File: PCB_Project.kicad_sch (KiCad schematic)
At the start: 0 parts

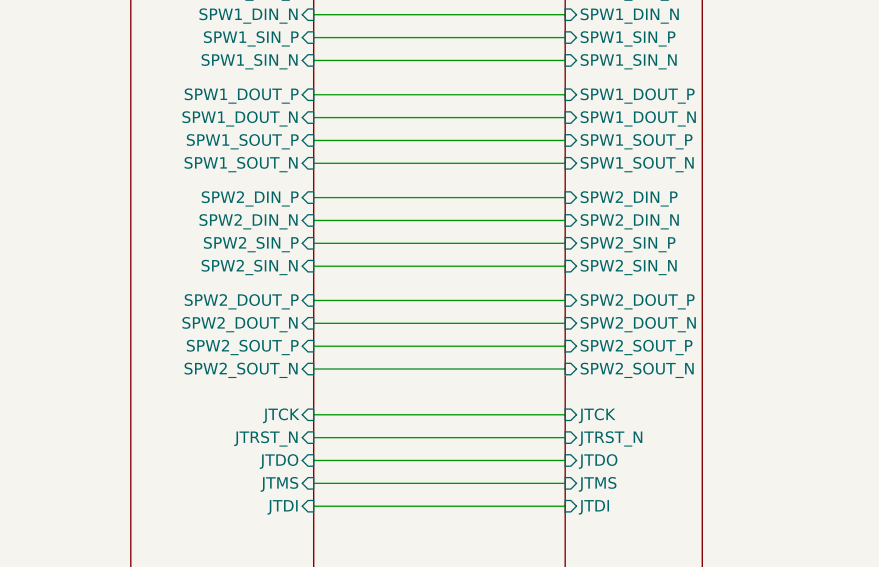
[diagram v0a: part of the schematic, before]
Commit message: added MAX, picoblade, NPN
added the LDO (placement), added the picoblade connector for CFG and deleted one SPW out of 2 in the DF9.
added the NPN transistor (placed)
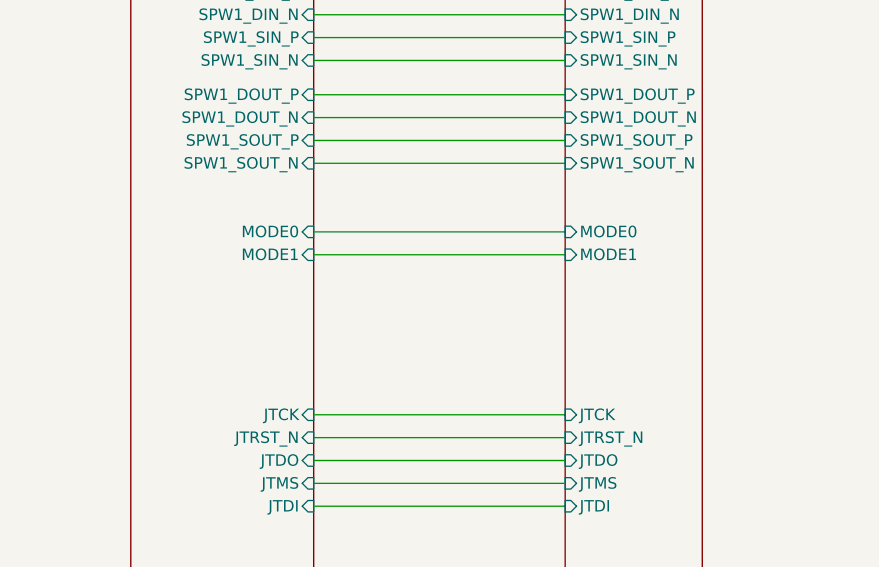
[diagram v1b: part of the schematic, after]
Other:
- sheet 02_FPGA_Config_JTAG_Bitstream_Reset ports: added MODE0, MODE1; removed SPW2_DIN_N, SPW2_DIN_P, SPW2_DOUT_N, SPW2_DOUT_P, SPW2_SIN_N, SPW2_SIN_P, SPW2_SOUT_N, SPW2_SOUT_P
- sheet DF9_CFG-SPW ports: added MODE0, MODE1; removed SPW2_DIN_N, SPW2_DIN_P, SPW2_DOUT_N, SPW2_DOUT_P, SPW2_SIN_N, SPW2_SIN_P, SPW2_SOUT_N, SPW2_SOUT_P
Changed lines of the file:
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@@
-	(wire
-		(pts
-			(xy 78.74 52.07) (xy 106.68 52.07)
-		)
-		(stroke
-			(width 0)
-			(type default)
-		)
-	)
 	(wire
 		(pts
@@
 	(wire
 		(pts
-			(xy 78.74 54.61) (xy 106.68 54.61)
-		)
-		(stroke
-			(width 0)
-			(type default)
-		)
-	)
-	(wire
-		(pts
 			(xy 78.74 48.26) (xy 106.68 48.26)
 		)
@@
 	(wire
 		(pts
-			(xy 78.74 57.15) (xy 106.68 57.15)
-		)
-		(stroke
-			(width 0)
-			(type default)
-		)
-	)
-	(wire
-		(pts
 			(xy 78.74 43.18) (xy 106.68 43.18)
 		)
@@
 	(wire
 		(pts
-			(xy 78.74 66.04) (xy 106.68 66.04)
-		)
-		(stroke
-			(width 0)
-			(type default)
-		)
-	)
-	(wire
-		(pts
 			(xy 78.74 36.83) (xy 106.68 36.83)
 		)
@@
 	(wire
 		(pts
-			(xy 78.74 68.58) (xy 106.68 68.58)
-		)
-		(stroke
-			(width 0)
-			(type default)
-		)
-	)
-	(wire
-		(pts
-			(xy 78.74 63.5) (xy 106.68 63.5)
+			(xy 78.74 58.42) (xy 106.68 58.42)
 		)
 		(stroke
@@
 	(wire
 		(pts
-			(xy 78.74 71.12) (xy 106.68 71.12)
-		)
-		(stroke
-			(width 0)
-			(type default)
-		)
-	)
-	(wire
-		(pts
-			(xy 78.74 59.69) (xy 106.68 59.69)
+			(xy 78.74 55.88) (xy 106.68 55.88)
 		)
 		(stroke
@@
 			)
 		)
-		(pin "SPW2_DIN_P" input
-			(at 106.68 52.07 180)
-			(effects
-				(font
-					(size 1.27 1.27)
-				)
-				(justify left)
-			)
-		)
-		(pin "SPW2_DOUT_P" input
-			(at 106.68 63.5 180)
-			(effects
-				(font
-					(size 1.27 1.27)
-				)
-				(justify left)
-			)
-		)
-		(pin "SPW2_SIN_N" input
-			(at 106.68 59.69 180)
-			(effects
-				(font
-					(size 1.27 1.27)
-				)
-				(justify left)
-			)
-		)
-		(pin "SPW2_DIN_N" input
-			(at 106.68 54.61 180)
-			(effects
-				(font
-					(size 1.27 1.27)
-				)
-				(justify left)
-			)
-		)
 		(pin "JTMS" input
 			(at 106.68 83.82 180)
@@
 			)
 		)
-		(pin "SPW2_DOUT_N" input
-			(at 106.68 66.04 180)
-			(effects
-				(font
-					(size 1.27 1.27)
-				)
-				(justify left)
-			)
-		)
 		(pin "JTDO" input
 			(at 106.68 81.28 180)
@@
 			)
 		)
-		(pin "SPW2_SOUT_P" input
-			(at 106.68 68.58 180)
-			(effects
-				(font
-					(size 1.27 1.27)
-				)
-				(justify left)
-			)
-		)
 		(pin "JTRST_N" input
 			(at 106.68 78.74 180)
@@
 			)
 		)
-		(pin "SPW2_SIN_P" input
-			(at 106.68 57.15 180)
-			(effects
-				(font
-					(size 1.27 1.27)
-				)
-				(justify left)
-			)
-		)
 		(pin "JTDI" input
 			(at 106.68 86.36 180)
@@
 			)
 		)
-		(pin "SPW2_SOUT_N" input
-			(at 106.68 71.12 180)
-			(effects
-				(font
-					(size 1.27 1.27)
-				)
-				(justify left)
-			)
-		)
 		(pin "JTCK" input
 			(at 106.68 76.2 180)
+			(effects
+				(font
+					(size 1.27 1.27)
+				)
+				(justify left)
+			)
+		)
+		(pin "MODE0" input
+			(at 106.68 55.88 180)
+			(effects
+				(font
+					(size 1.27 1.27)
+				)
+				(justify left)
+			)
+		)
+		(pin "MODE1" input
+			(at 106.68 58.42 180)
 			(effects
 				(font
@@
 			)
 		)
-		(pin "SPW2_DOUT_N" input
-			(at 78.74 66.04 0)
-			(effects
-				(font
-					(size 1.27 1.27)
-				)
-				(justify right)
-			)
-		)
 		(pin "JTMS" input
 			(at 78.74 83.82 0)
@@
 			)
 		)
-		(pin "SPW2_SOUT_P" input
-			(at 78.74 68.58 0)
-			(effects
-				(font
-					(size 1.27 1.27)
-				)
-				(justify right)
-			)
-		)
-		(pin "SPW2_DIN_N" input
-			(at 78.74 54.61 0)
-			(effects
-				(font
-					(size 1.27 1.27)
-				)
-				(justify right)
-			)
-		)
-		(pin "SPW2_SIN_N" input
-			(at 78.74 59.69 0)
-			(effects
-				(font
-					(size 1.27 1.27)
-				)
-				(justify right)
-			)
-		)
-		(pin "SPW2_SOUT_N" input
-			(at 78.74 71.12 0)
-			(effects
-				(font
-					(size 1.27 1.27)
-				)
-				(justify right)
-			)
-		)
-		(pin "SPW2_SIN_P" input
-			(at 78.74 57.15 0)
-			(effects
-				(font
-					(size 1.27 1.27)
-				)
-				(justify right)
-			)
-		)
-		(pin "SPW2_DIN_P" input
-			(at 78.74 52.07 0)
-			(effects
-				(font
-					(size 1.27 1.27)
-				)
-				(justify right)
-			)
-		)
-		(pin "SPW2_DOUT_P" input
-			(at 78.74 63.5 0)
-			(effects
-				(font
+		(pin "MODE0" input
+			(at 78.74 55.88 0)
+			(effects
+				(font
+					(size 1.27 1.27)
+				)
+				(justify right)
+			)
+		)
+		(pin "MODE1" input
+			(at 78.74 58.42 0)
+			(effects
+				(font

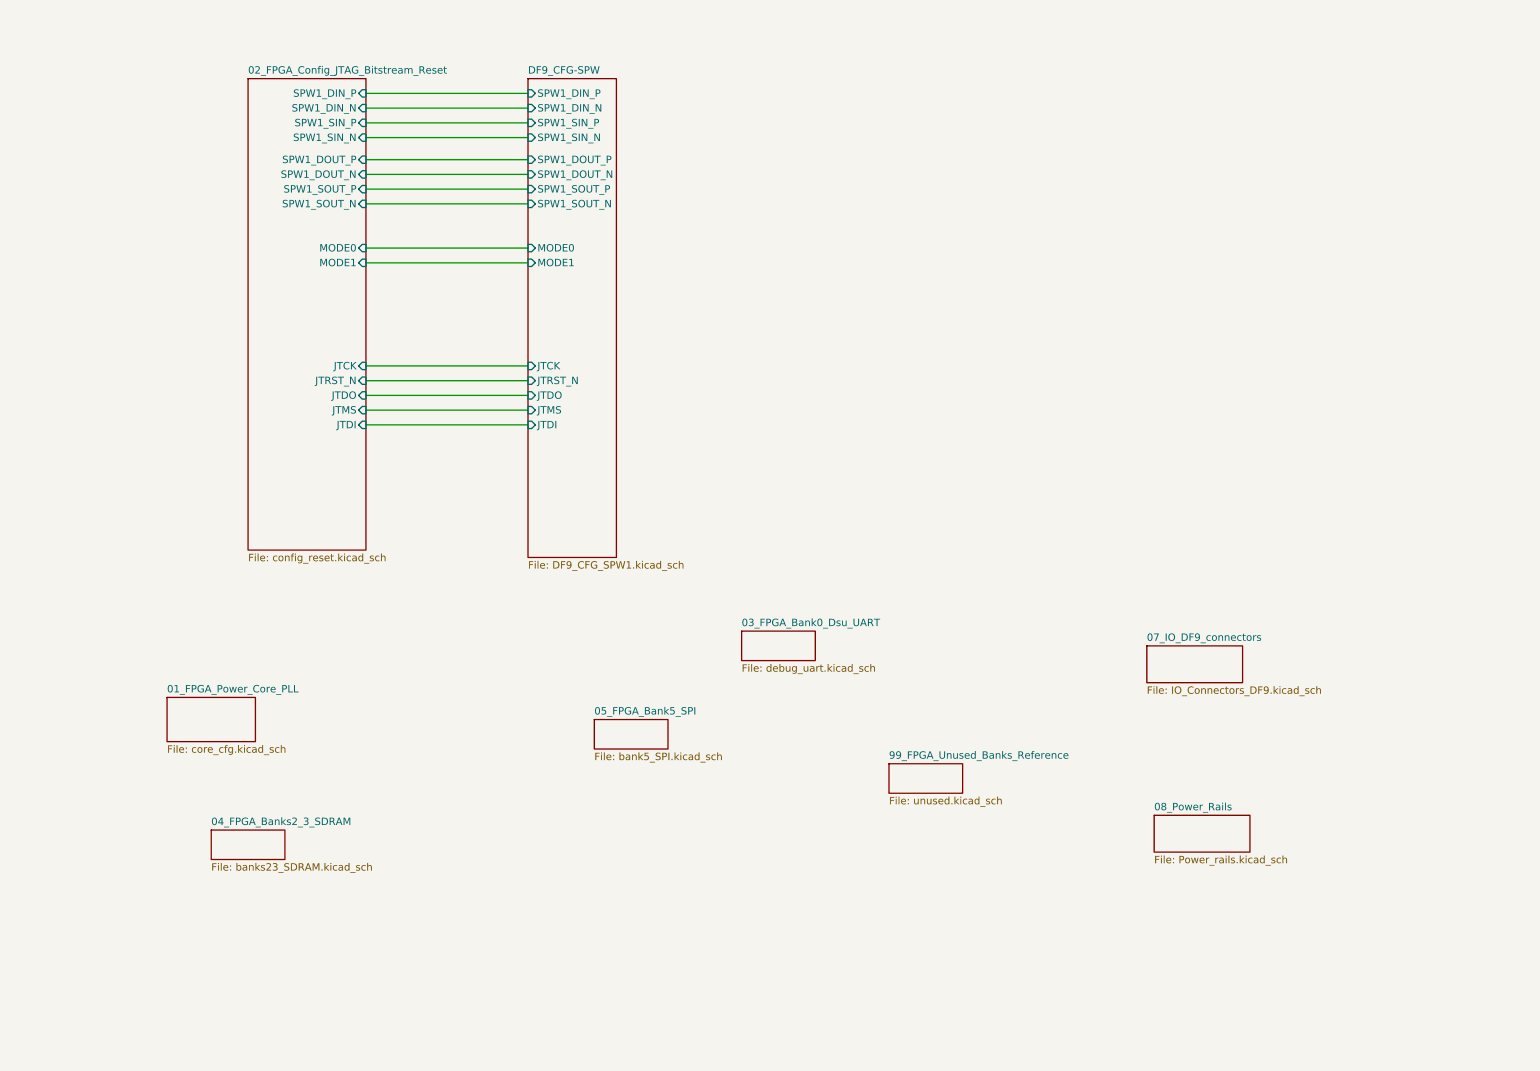
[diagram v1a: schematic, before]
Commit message: CFG, bga sdram, banks to connectors, docoupling
Finished completely routing bga sdram, finished tracing Banks to connectors DF9. Finished tracing Picoblade, diode, reset supervisor. Finished tracing LEDS on bank 5. Finished decoupling all banks and core. Missing only the power tree and power rail level decoupling.
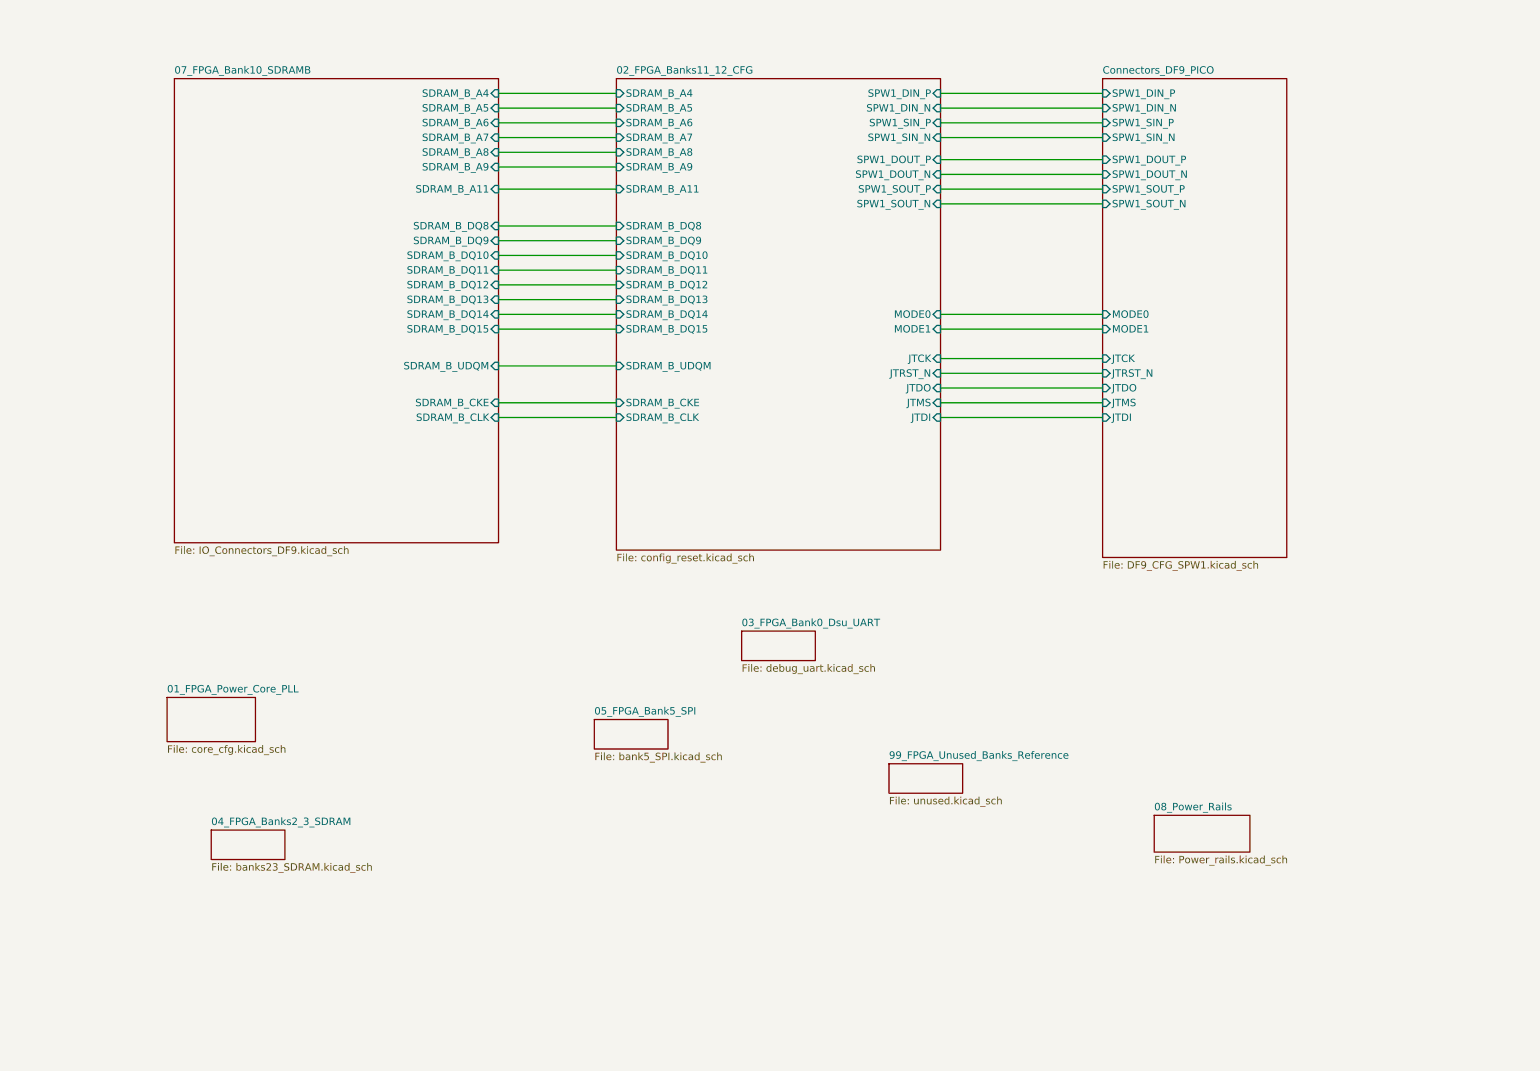
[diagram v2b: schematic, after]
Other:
- sheet 02_FPGA_Config_JTAG_Bitstream_Reset renamed 02_FPGA_Banks11_12_CFG
- sheet 07_IO_DF9_connectors renamed 07_FPGA_Bank10_SDRAMB
- sheet DF9_CFG-SPW renamed Connectors_DF9_PICO
- sheet 02_FPGA_Banks11_12_CFG ports: added SDRAM_B_A11, SDRAM_B_A4, SDRAM_B_A5, SDRAM_B_A6, SDRAM_B_A7, SDRAM_B_A8, SDRAM_B_A9, SDRAM_B_CKE, SDRAM_B_CLK, SDRAM_B_DQ10, SDRAM_B_DQ11, SDRAM_B_DQ12, SDRAM_B_DQ13, SDRAM_B_DQ14, SDRAM_B_DQ15, SDRAM_B_DQ8, SDRAM_B_DQ9, SDRAM_B_UDQM; removed none
- sheet 07_FPGA_Bank10_SDRAMB ports: added SDRAM_B_A11, SDRAM_B_A4, SDRAM_B_A5, SDRAM_B_A6, SDRAM_B_A7, SDRAM_B_A8, SDRAM_B_A9, SDRAM_B_CKE, SDRAM_B_CLK, SDRAM_B_DQ10, SDRAM_B_DQ11, SDRAM_B_DQ12, SDRAM_B_DQ13, SDRAM_B_DQ14, SDRAM_B_DQ15, SDRAM_B_DQ8, SDRAM_B_DQ9, SDRAM_B_UDQM; removed none

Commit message: power tree
power tree defined. Few changes remaining but almost finalized
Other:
- sheet 01_FPGA_Power_Core_PLL renamed FPGA_Core_PLL
- sheet 02_FPGA_Banks11_12_CFG renamed FPGA_Banks11_12_CFG
- sheet 03_FPGA_Bank0_Dsu_UART renamed FPGA_Bank0
- sheet 04_FPGA_Banks2_3_SDRAM renamed FPGA_Banks2_3_SDRAM
- sheet 05_FPGA_Bank5_SPI renamed FPGA_Bank5_SPI
- sheet 07_FPGA_Bank10_SDRAMB renamed FPGA_Bank10_SDRAMB
- sheet 08_Power_Rails renamed Rails_Decoupling
- sheet 99_FPGA_Unused_Banks_Reference renamed Power_Tree_LDOs
- sheet Connectors_DF9_PICO ports: added B0_01N_DF9, B0_01P_DF9, B0_02N_DF9, B0_02P_DF9, B0_03N_DF9, B0_03P_DF9, B0_04N_DF9, B0_04P_DF9, B0_05P_DF9, B0_06N_DF9, B0_06P_DF9, B0_07N_DF9, B0_07P_DF9, B0_08P_DF9, B0_09N_DF9, B0_09P_DF9, B0_10N_DF9, B0_10P_DF9, B0_11P_DF9, B5_03N_DF9, B5_03P_DF9, B5_04N_DF9, B5_07N_DF9, B5_08N_DF9, B5_08P_DF9, B5_09N_DF9, B5_10N_DF9, B5_10P_DF9, B5_11N_DF9, B5_11P_DF9, B5_12N_DF9, B5_12P_DF9, B5_13N_DF9; removed none
- sheet FPGA_Bank0 ports: added B0_01N_DF9, B0_01P_DF9, B0_02N_DF9, B0_02P_DF9, B0_03N_DF9, B0_03P_DF9, B0_04N_DF9, B0_04P_DF9, B0_05P_DF9, B0_06N_DF9, B0_06P_DF9, B0_07N_DF9, B0_07P_DF9, B0_08P_DF9, B0_09N_DF9, B0_09P_DF9, B0_10N_DF9, B0_10P_DF9, B0_11P_DF9; removed none
- sheet FPGA_Bank5_SPI ports: added B5_03N_DF9, B5_03P_DF9, B5_04N_DF9, B5_07N_DF9, B5_08N_DF9, B5_08P_DF9, B5_09N_DF9, B5_10N_DF9, B5_10P_DF9, B5_11N_DF9, B5_11P_DF9, B5_12N_DF9, B5_12P_DF9, B5_13N_DF9; removed none

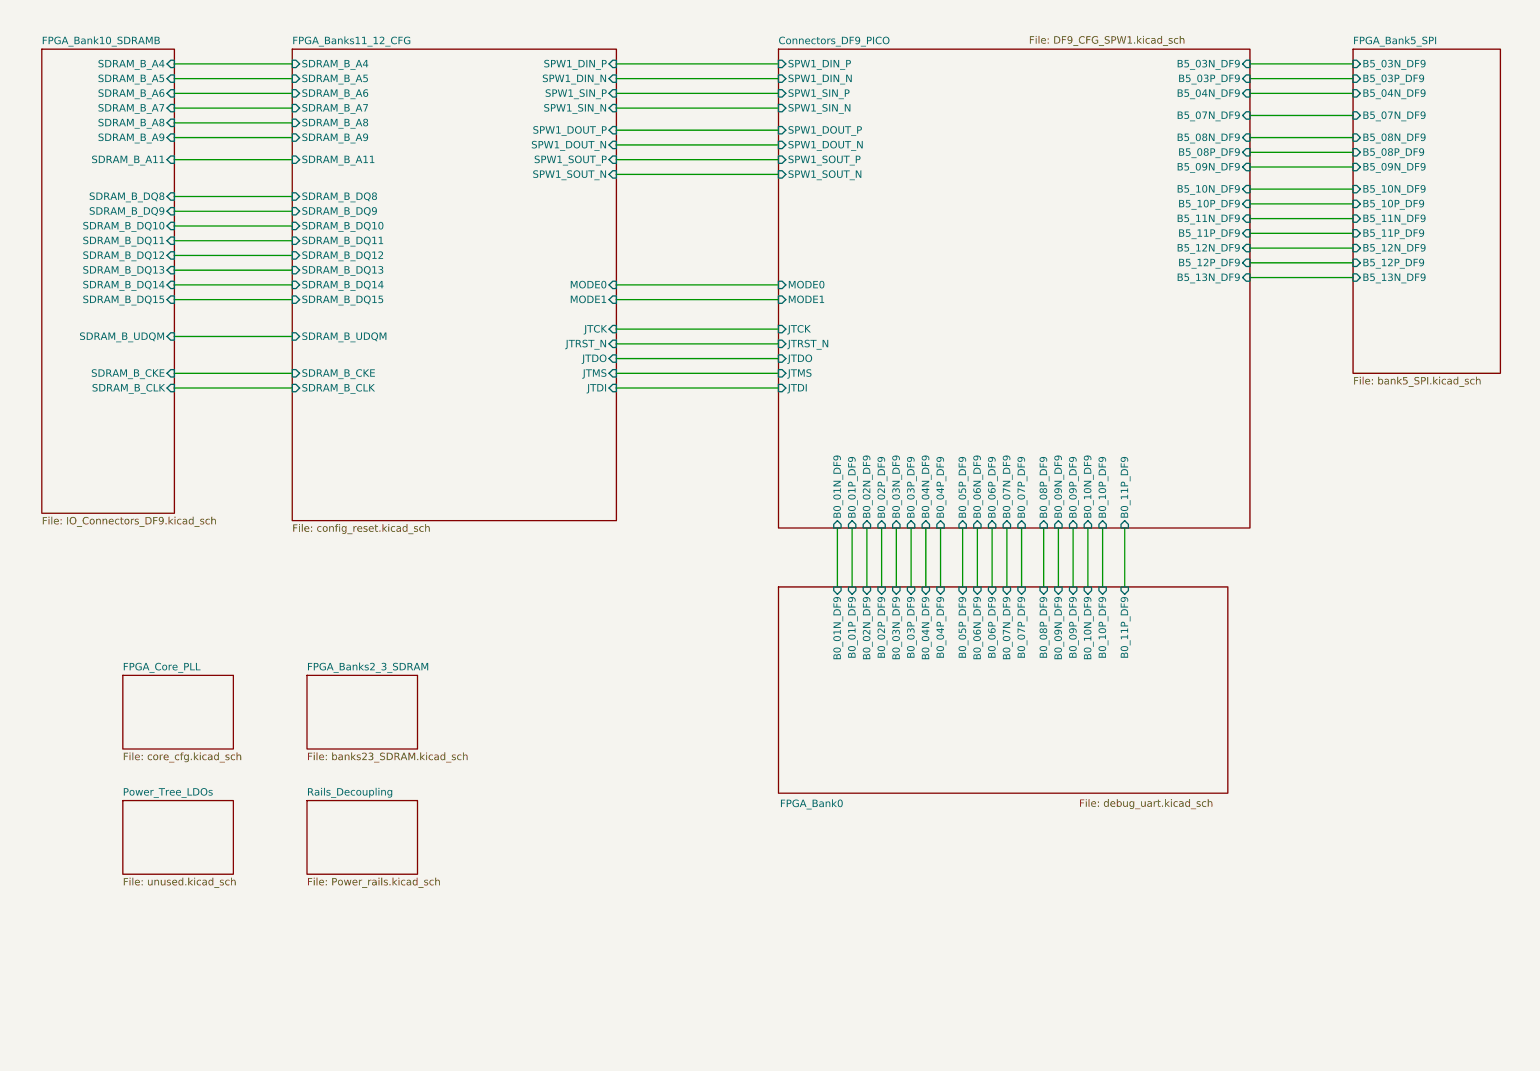
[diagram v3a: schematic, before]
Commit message: pre order adjustments. Board symmetry
adjusted little things brought up by DFM checker of JLCPCB. Board's edges fully symmetrical on y axis. 2mm shift on x axis of the DF9s maintained
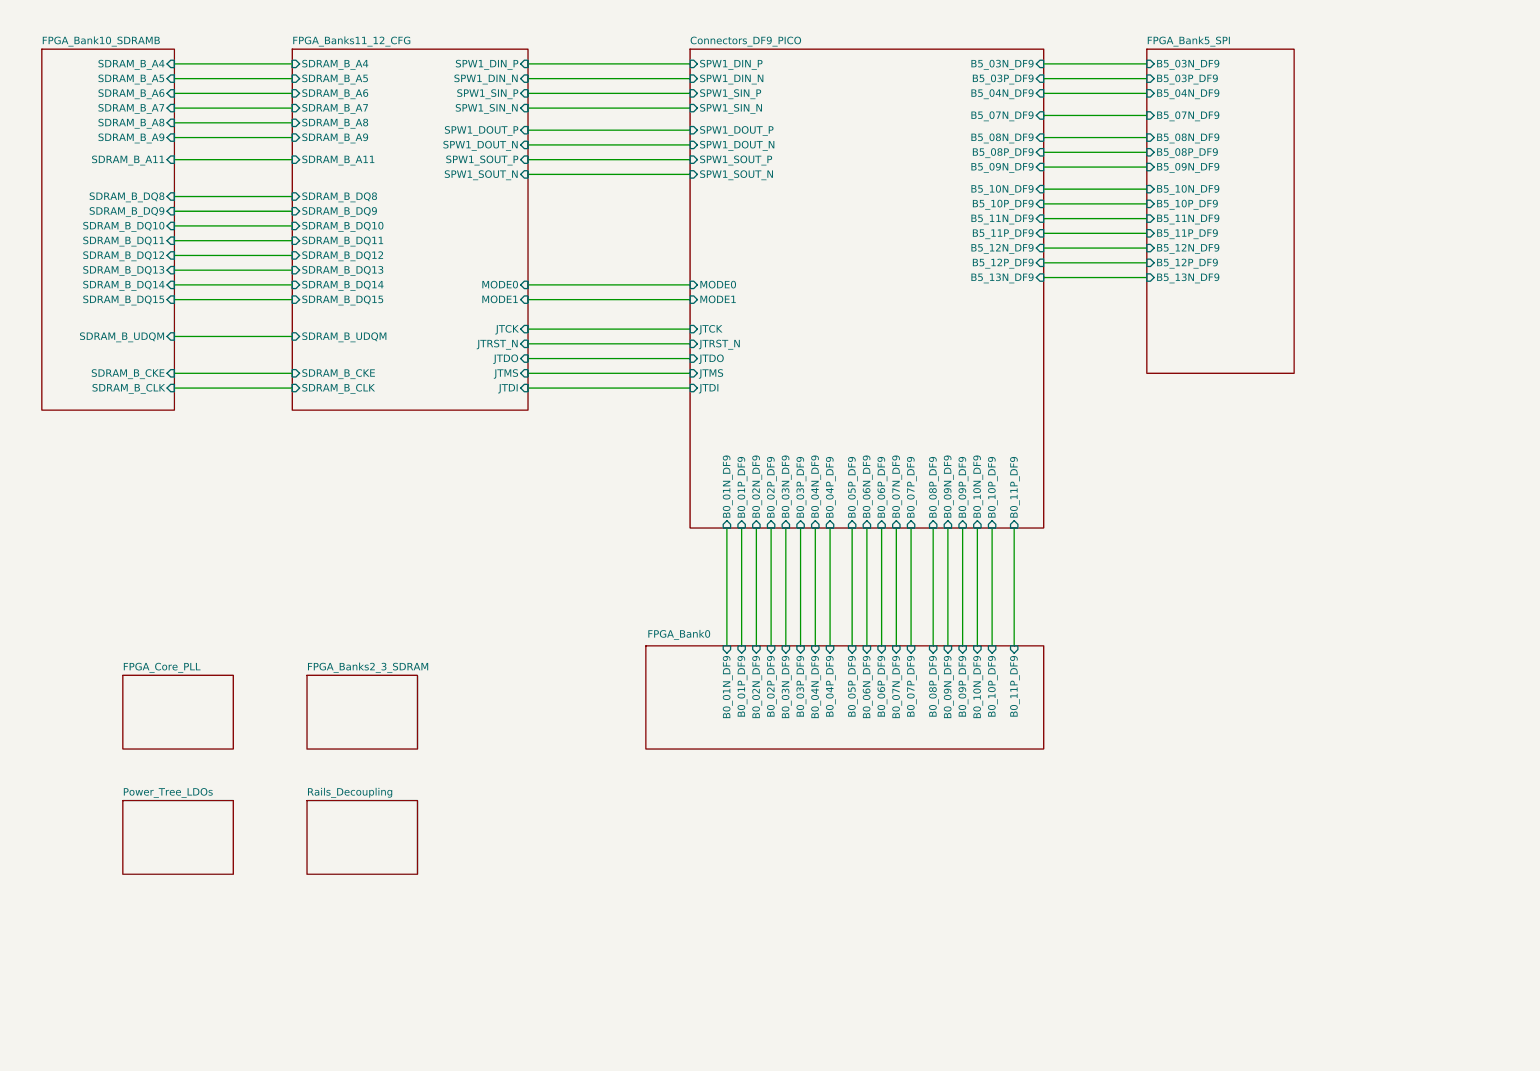
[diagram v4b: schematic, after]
